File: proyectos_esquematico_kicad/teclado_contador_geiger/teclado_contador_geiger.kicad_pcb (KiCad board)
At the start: 2 copper layers, 16 parts, among them J1 Conn_01x05_Female, SW1 SW_SPST, SW2 SW_SPST, SW3 SW_SPST, SW4 SW_SPST, SW5 SW_SPST, SW6 SW_SPST

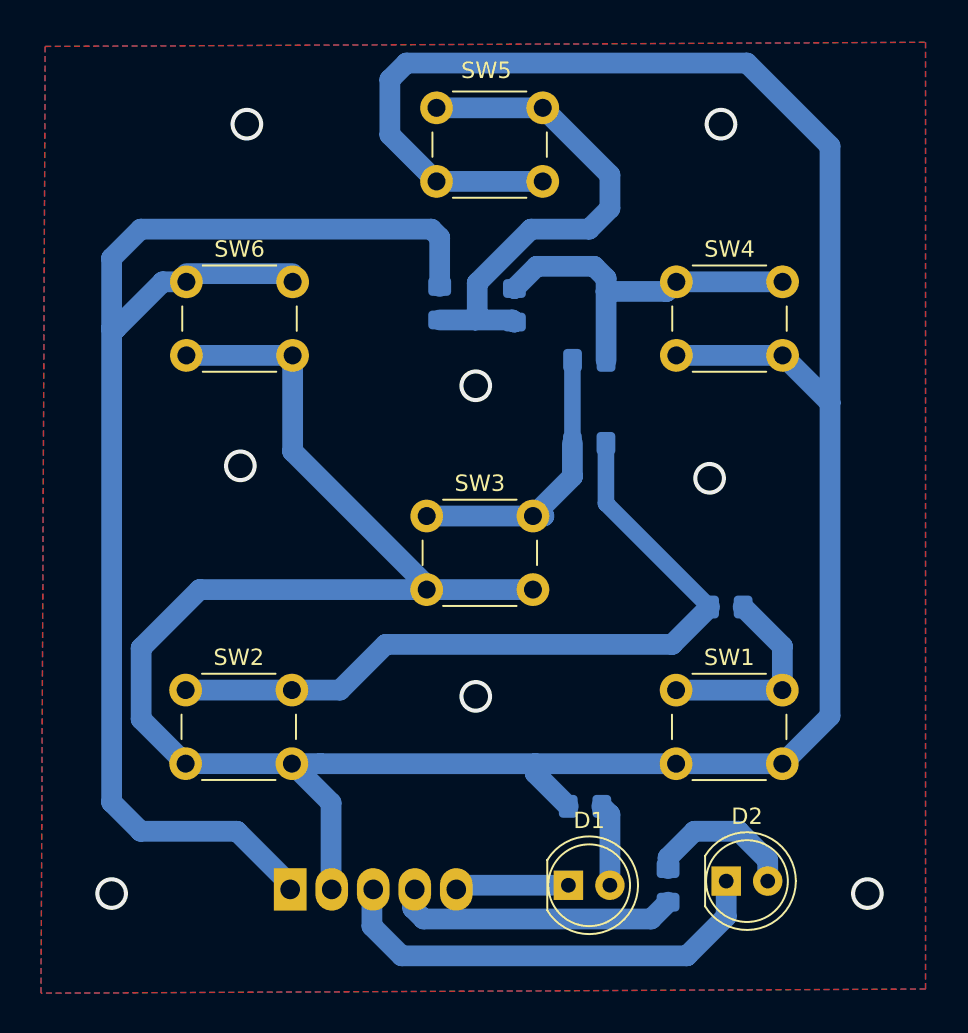
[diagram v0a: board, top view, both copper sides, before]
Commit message: Modificaciones en el PCB para poder mardarlo a hacer al LCI. Agregado del esquematico del Arduino UNO R3 actualizado a la carpeta 'doc'
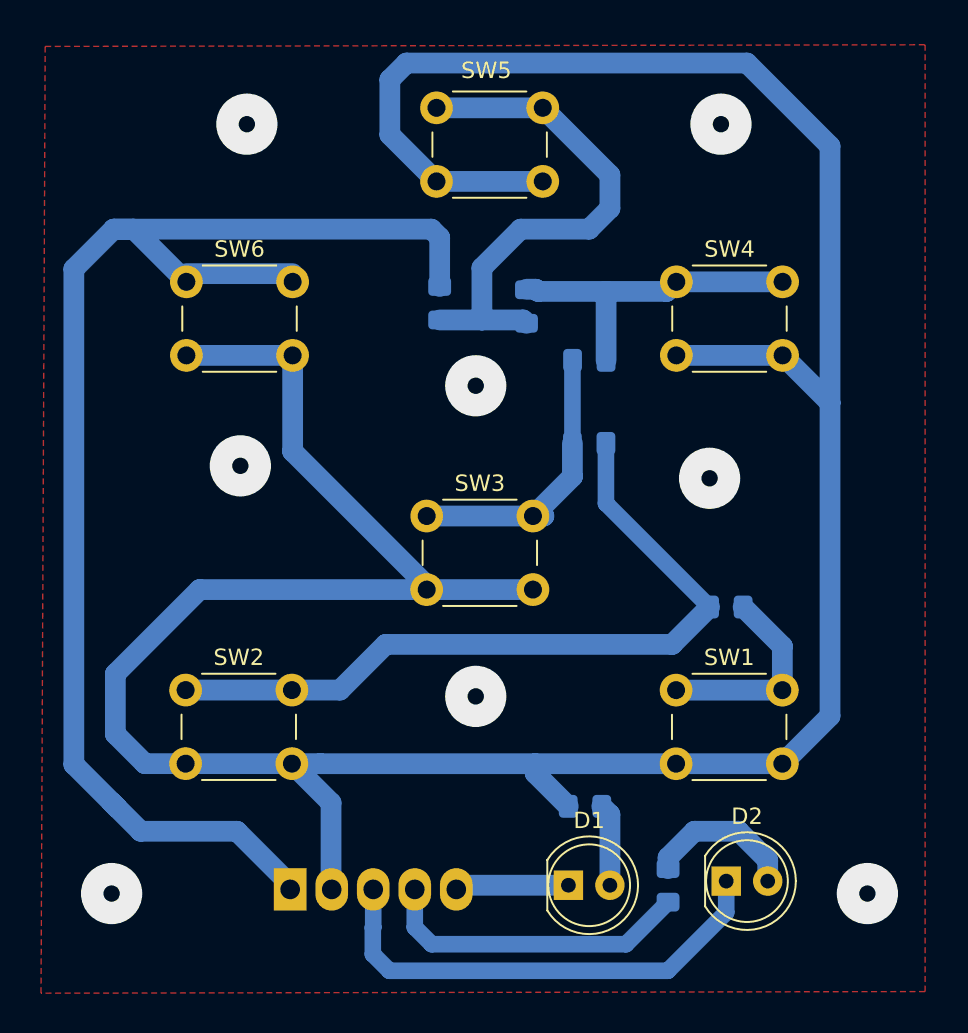
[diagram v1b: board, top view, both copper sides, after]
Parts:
- moved R4 0.74 mm to (135.1, 63.2)
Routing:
- net /teclado_out: track 83.0 -> 86.3 mm
- net +5V: track 199.9 -> 202.7 mm
- net Net-(R3-Pad2): track 22.6 -> 20.2 mm
- net Net-(J1-Pad4): track 17.5 -> 19.3 mm
- net GND: track 27.8 -> 29.4 mm, vias 8 -> 0
- net Net-(R4-Pad2): track 31.3 -> 32.3 mm
- net (no net): vias 0 -> 8
- removed copper zone on B.Cu, net GND
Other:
- net class Default: clearance 1 -> 0.6096; trace_width 0.25 -> 1.27; via_dia 0.8 -> 3.746; via_drill 0.4 -> 1
- rule trace_clearance: 1 -> 0.6096
- rule trace_min: 0.2 -> 0.4064
- rule via_min_drill: 0.3 -> 1
- rule via_min_size: 0.4 -> 1.778

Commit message: Actualizacion de los gerbers y de los drills (cambios necesarios para poder mandar a hacer las placas al LCI)
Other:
- board outline added: 55 x 59 mm
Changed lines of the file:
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@@
   (page A4)
   (layers
-    (0 F.Cu signal hide)
+    (0 F.Cu signal)
     (31 B.Cu signal)
     (32 B.Adhes user)
@@
     (visible_elements 7FFFFFFF)
     (pcbplotparams
-      (layerselection 0x010fc_ffffffff)
+      (layerselection 0x01000_ffffffff)
       (usegerberextensions false)
       (usegerberattributes false)
@@
     )
   )
-  (gr_line (start 105 105.504) (end 160 105.504) (layer B.Mask) (width 0.2))
-  (gr_line (start 160 46.504) (end 160 105.504) (layer B.Mask) (width 0.2))
-  (gr_line (start 105 46.504) (end 105 105.504) (layer B.Mask) (width 0.2))
-  (gr_line (start 105 46.504) (end 160 46.504) (layer B.Mask) (width 0.2))
+  (gr_line (start 105 105.504) (end 160 105.504) (layer Edge.Cuts) (width 0.2))
+  (gr_line (start 160 46.504) (end 160 105.504) (layer Edge.Cuts) (width 0.2))
+  (gr_line (start 105 46.504) (end 105 105.504) (layer Edge.Cuts) (width 0.2))
+  (gr_line (start 105 46.504) (end 160 46.504) (layer Edge.Cuts) (width 0.2))
+  (via (at 109.728 99.06) (size 3.746) (drill 1) (layers F.Cu B.Cu) (net 0))
+  (via (at 132 68) (size 3.746) (drill 1) (layers F.Cu B.Cu) (net 0))
+  (via (at 147 52) (size 3.746) (drill 1) (layers F.Cu B.Cu) (net 0))
+  (via (at 155.956 99.06) (size 3.746) (drill 1) (layers F.Cu B.Cu) (net 0))
+  (via (at 117.602 72.898) (size 3.746) (drill 1) (layers F.Cu B.Cu) (net 0))
+  (via (at 146.304 73.66) (size 3.746) (drill 1) (layers F.Cu B.Cu) (net 0))
+  (via (at 118 52) (size 3.746) (drill 1) (layers F.Cu B.Cu) (net 0))
+  (via (at 132 87) (size 3.746) (drill 1) (layers F.Cu B.Cu) (net 0))
   (segment (start 130.904 98.552) (end 130.65 98.806) (width 1.27) (layer B.Cu) (net 1))
   (segment (start 137.668 98.552) (end 130.904 98.552) (width 1.27) (layer B.Cu) (net 1))
@@
   (segment (start 115.112 80.468) (end 129.254 80.468) (width 1.27) (layer B.Cu) (net 3))
   (segment (start 129.6 55.5) (end 136.1 55.5) (width 1.27) (layer B.Cu) (net 3))
-  (via (at 109.728 99.06) (size 3.746) (drill 1) (layers F.Cu B.Cu) (net 0))
-  (via (at 132 68) (size 3.746) (drill 1) (layers F.Cu B.Cu) (net 0))
-  (via (at 147 52) (size 3.746) (drill 1) (layers F.Cu B.Cu) (net 0))
-  (via (at 155.956 99.06) (size 3.746) (drill 1) (layers F.Cu B.Cu) (net 0))
-  (via (at 117.602 72.898) (size 3.746) (drill 1) (layers F.Cu B.Cu) (net 0))
-  (via (at 146.304 73.66) (size 3.746) (drill 1) (layers F.Cu B.Cu) (net 0))
-  (via (at 118 52) (size 3.746) (drill 1) (layers F.Cu B.Cu) (net 0))
-  (via (at 132 87) (size 3.746) (drill 1) (layers F.Cu B.Cu) (net 0))
   (segment (start 114.254 91.114) (end 111.7642 91.114) (width 1.27) (layer B.Cu) (net 3))
   (segment (start 111.7642 91.114) (end 109.9566 89.3064) (width 1.27) (layer B.Cu) (net 3))
